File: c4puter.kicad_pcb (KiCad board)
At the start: 6 copper layers, 200 x 200 mm, 252 parts, among them J1 PDI, J2 MICROSD, J7 19V 3A, J8 DEBUG, Q1 AOD4189, Q2 AOD4189, Q3 2N7002, Q4 DMN3016LDN, Q5 DMN3016LDN, Q6 ULN2003APWR, Q7 ULN2003APWR, Q8 DMN3016LDN, Q9 DMN3018SSS, SW1 POWER, SW2 SW, U1 ATXMEGA8E5-MU, U4 TPIC6B595DW

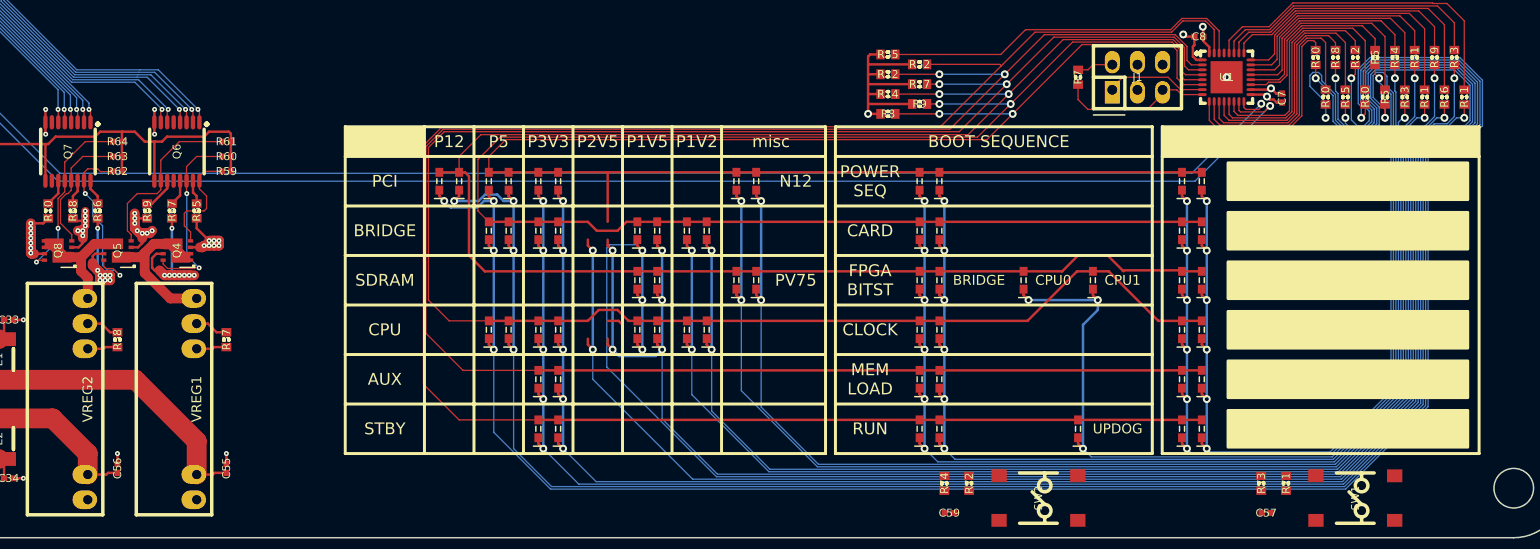
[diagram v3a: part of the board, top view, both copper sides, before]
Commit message: Delete extra column of LEDs
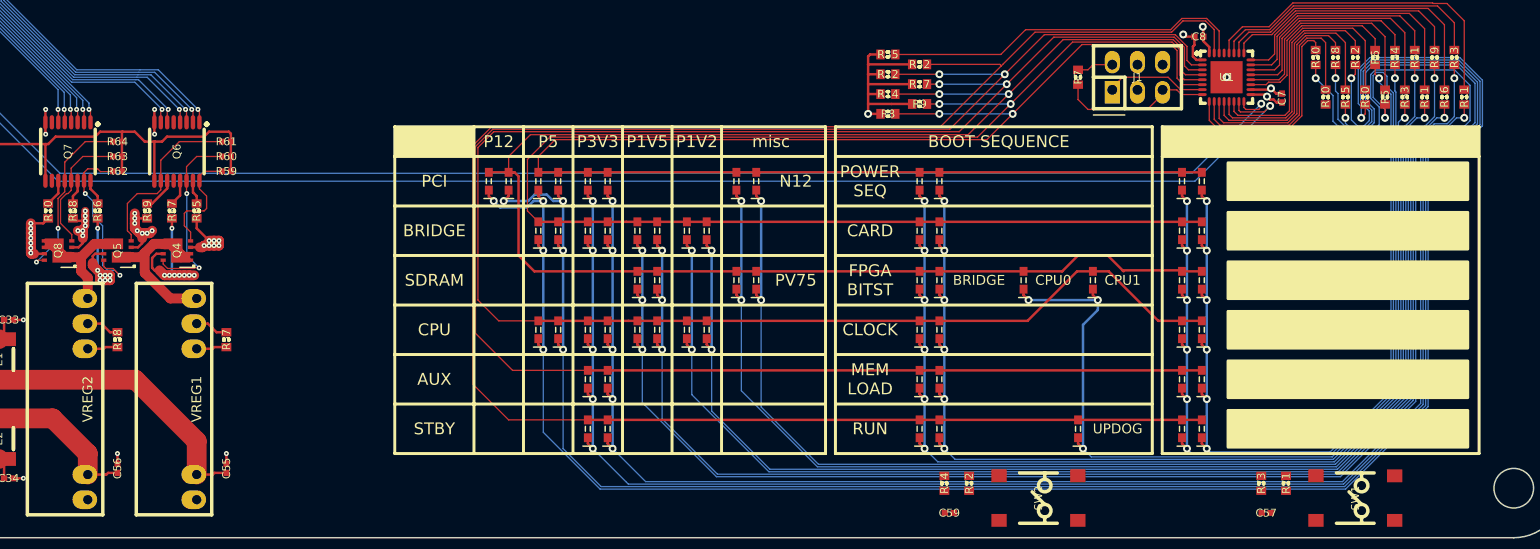
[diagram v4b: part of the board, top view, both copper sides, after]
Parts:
- moved DS1 5.00 mm to (91.5, 164.0)
- moved DS10 5.00 mm to (101.5, 169.0)
- moved DS11 5.00 mm to (101.5, 179.0)
- moved DS12 5.00 mm to (101.5, 184.0)
- moved DS13 5.00 mm to (101.5, 189.0)
- moved DS14 5.00 mm to (103.5, 164.0)
- moved DS15 5.00 mm to (103.5, 169.0)
- moved DS16 5.00 mm to (103.5, 179.0)
- moved DS17 5.00 mm to (103.5, 184.0)
- moved DS18 5.00 mm to (103.5, 189.0)
- moved DS2 5.00 mm to (93.5, 164.0)
- moved DS3 5.00 mm to (96.5, 164.0)
- moved DS4 5.00 mm to (96.5, 169.0)
- moved DS5 5.00 mm to (96.5, 179.0)
- moved DS6 5.00 mm to (98.5, 164.0)
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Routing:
- net /Blinkenlights/COL4: track 177.1 -> 0.00 mm, vias 3 -> 0
- net /Blinkenlights/COL6: track 153.6 -> 135.4 mm, vias 6 -> 4
- net /Blinkenlights/ROW4: track 201.2 -> 185.0 mm
- net /Blinkenlights/COL5: track 183.5 -> 167.8 mm
- net /Blinkenlights/ROW0: track 170.5 -> 155.5 mm
- net /Blinkenlights/ROW3: track 192.7 -> 181.8 mm
- net /Blinkenlights/ROW1: track 169.1 -> 158.3 mm
- net /Blinkenlights/ROW2: track 183.1 -> 173.1 mm
- net /Blinkenlights/ROW5: track 199.6 -> 189.6 mm
- net /Blinkenlights/COL1: track 197.2 -> 192.2 mm
- net /Blinkenlights/COL3: track 186.5 -> 181.5 mm
- net /Blinkenlights/COL2: track 184.7 -> 179.7 mm
- net /Blinkenlights/COL0: track 191.6 -> 186.6 mm
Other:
- board text removed: "P2V5"

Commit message: workworkwork
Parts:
- removed R14, R17, R22, R52, R55, R8, R9: 51k, IPC7351-Nominal:RESC1608X50
- added C82: 1u, IPC7351-Nominal:CAPC1005X55, F.Cu at (136.5, 134.5)
- added C83: 1u, IPC7351-Nominal:CAPC1005X55, F.Cu at (194.2, 130.5)
- added C84: 1u, IPC7351-Nominal:CAPC1005X55, F.Cu at (190.5, 130.5)
- added C85: 1u, IPC7351-Nominal:CAPC1005X55, F.Cu at (191.8, 130.5)
- added C86: 1u, IPC7351-Nominal:CAPC1005X55, F.Cu at (193.0, 130.5)
- added C87: 1u, IPC7351-Nominal:CAPC1005X55, F.Cu at (195.5, 138.5)
- added C88: 1u, IPC7351-Nominal:CAPC1005X55, F.Cu at (54.2, 21.5)
- added C89: 1u, IPC7351-Nominal:CAPC1005X55, F.Cu at (54.2, 19.2)
- added JP1: JUMPER-SOLDER, conn-test:JUMPER-SOLDER-SMD, F.Cu at (192.0, 100.0)
- added JP10: JUMPER-SOLDER, conn-test:JUMPER-SOLDER-SMD, F.Cu at (120.0, 115.0)
- added JP11: JUMPER-SOLDER, conn-test:JUMPER-SOLDER-SMD, F.Cu at (120.0, 118.0)
- added JP12: JUMPER-SOLDER, conn-test:JUMPER-SOLDER-SMD, F.Cu at (171.0, 100.5)
- added JP13: JUMPER-SOLDER, conn-test:JUMPER-SOLDER-SMD, F.Cu at (120.0, 112.0)
- added JP2: JUMPER-SOLDER, conn-test:JUMPER-SOLDER-SMD, F.Cu at (159.0, 100.5)
- added JP3: JUMPER-SOLDER, conn-test:JUMPER-SOLDER-SMD, F.Cu at (186.5, 100.0)
- added JP4: JUMPER-SOLDER, conn-test:JUMPER-SOLDER-SMD, F.Cu at (44.0, 101.0)
- added JP5: JUMPER-SOLDER, conn-test:JUMPER-SOLDER-SMD, F.Cu at (44.0, 97.0)
- added JP6: JUMPER-SOLDER, conn-test:JUMPER-SOLDER-SMD, F.Cu at (44.0, 105.0)
- added JP7: JUMPER-SOLDER, conn-test:JUMPER-SOLDER-SMD, F.Cu at (195.0, 100.0)
- added JP8: JUMPER-SOLDER, conn-test:JUMPER-SOLDER-SMD, F.Cu at (132.0, 100.0)
- added JP9: JUMPER-SOLDER, conn-test:JUMPER-SOLDER-SMD, F.Cu at (147.0, 100.5)
- added Q10: AOD514, smd-semi:TO-252, F.Cu at (180.3, 117.0)
- added Q11: AOD514, smd-semi:TO-252, F.Cu at (167.0, 118.0)
- added R75: 100k, IPC7351-Nominal:RESC1005X40, F.Cu at (150.0, 144.5)
- added R76: 100k, IPC7351-Nominal:RESC1005X40, F.Cu at (151.5, 144.5)
- added R77: R01, IPC7351-Nominal:RESC2012X50, F.Cu at (192.0, 104.0)
- added R78: R001, manuf:VISHAY-WSL3637-LARGE, F.Cu at (153.0, 107.0)
- added R79: R001, manuf:VISHAY-WSL3637-LARGE, F.Cu at (180.0, 107.0)
- added R80: R20, IPC7351-Nominal:RESC2012X50, F.Cu at (195.0, 104.0)
- added R81: R01, IPC7351-Nominal:RESC2012X50, F.Cu at (132.0, 104.0)
- added R82: R001, manuf:VISHAY-WSL3637-LARGE, F.Cu at (141.0, 107.0)
- added R83: R01, IPC7351-Nominal:RESC2012X50, F.Cu at (124.0, 115.0)
- added R84: R001, manuf:VISHAY-WSL3637-LARGE, F.Cu at (165.0, 107.0)
- added R85: 1k, IPC7351-Nominal:RESC1005X40, F.Cu at (190.5, 133.0)
- added U2: PCF8575, IPC7351-Nominal:SOP65P775X200-24, F.Cu at (140.0, 140.0)
- added U3: PCF8523TK, IPC7351-Nominal:SON80P400X400X80-9, F.Cu at (194.5, 134.5)
- added U5: CDCE913PW, IPC7351-Nominal:SOP65P640X120-14, F.Cu at (59.1, 19.3)
- added W1: NET-TIE, conn-test:NET-TIE-0.2mm, B.Cu at (33.8, 190.6)
- added W2: NET-TIE, conn-test:NET-TIE-0.2mm, B.Cu at (33.4, 178.6)
- added W3: NET-TIE, conn-test:NET-TIE-0.2mm, B.Cu at (33.8, 166.6)
- added W4: NET-TIE, conn-test:NET-TIE-0.2mm, B.Cu at (33.4, 156.6)
- added W5: NET-TIE, conn-test:NET-TIE-0.2mm, B.Cu at (33.5, 148.5)
- added X1: 32768, manuf:CITIZEN-CM130, F.Cu at (194.5, 140.5)
- added X2: 20MHz, IPC7351-Nominal:XTAL1200X480X460, F.Cu at (59.0, 13.1)
- Q4, Q5: value DMN3016LDN -> 2N7002; footprint manuf:DIODES-V-DFN3030-8 -> smd-semi:SOT-23
- Q6: value ULN2003APWR -> 2N7002; footprint IPC7351-Nominal:SOP65P640X120-16 -> smd-semi:SOT-23
- Q8: value DMN3016LDN -> ULN2003APWR; footprint manuf:DIODES-V-DFN3030-8 -> IPC7351-Nominal:SOP65P640X120-16
- Q9: value DMN3018SSS -> AOD417; footprint IPC7351-Nominal:SOIC127P600X175-8 -> smd-semi:TO-252
- R59, R60, R61: value 330k -> 0R
- R62, R63, R64: value 330k -> 120; footprint IPC7351-Nominal:RESC1005X40 -> IPC7351-Nominal:RESC1608X50
- R65, R66, R67, R69, R70: value 100 -> 120
- R68: value 100 -> 100k; footprint IPC7351-Nominal:RESC1608X50 -> IPC7351-Nominal:RESC1005X40
- U4: value TPIC6B595DW -> TLV70218DBV; footprint IPC7351-Nominal:SOIC127P1030X265-20 -> smd-semi:SOT-23-5
- moved U4 201.8 mm to (51.2, 20.2)
- moved Q9 155.0 mm to (190.0, 114.0), turned to 90 degrees
- moved R70 116.9 mm to (160.5, 139.0), turned to 180 degrees
- moved Q8 108.8 mm to (150.0, 133.0), turned to 0 degrees
- moved R69 107.8 mm to (160.5, 137.0), turned to 180 degrees
- moved R66 107.7 mm to (157.0, 143.0), turned to 180 degrees
- moved R62 107.6 mm to (157.0, 132.0), turned to 180 degrees
- moved R63 105.9 mm to (157.0, 137.0), turned to 180 degrees
- moved R64 105.1 mm to (157.0, 139.0), turned to 180 degrees
- moved R67 104.3 mm to (157.0, 130.0), turned to 180 degrees
- moved Q7 103.2 mm to (150.0, 140.0), turned to 0 degrees
- moved R68 101.5 mm to (148.5, 144.5)
- moved R65 98.5 mm to (157.0, 141.0), turned to 180 degrees
- moved Q5 93.5 mm to (138.0, 130.0)
- moved Q6 87.7 mm to (142.0, 130.0), turned to 90 degrees
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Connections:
- net /Power/3V3_2 renamed +3VB
- net /Power/5V_2 renamed +5VB
- net /Power/N12V renamed -12
- net N12_PCI renamed N12V_PCI
- net P12_PCI renamed P12V_PCI
- BRIDGE1 pad J10: P1V2_BRIDGE -> P1V2_CORE
- BRIDGE1 pad J12: P1V2_BRIDGE -> P1V2_CORE
- BRIDGE1 pad J14: P1V2_BRIDGE -> P1V2_CORE
- BRIDGE1 pad J8: P1V2_BRIDGE -> P1V2_CORE
- BRIDGE1 pad K11: P1V2_BRIDGE -> P1V2_CORE
- BRIDGE1 pad K13: P1V2_BRIDGE -> P1V2_CORE
- BRIDGE1 pad K9: P1V2_BRIDGE -> P1V2_CORE
- BRIDGE1 pad L10: P1V2_BRIDGE -> P1V2_CORE
- BRIDGE1 pad L12: P1V2_BRIDGE -> P1V2_CORE
- BRIDGE1 pad L14: P1V2_BRIDGE -> P1V2_CORE
- BRIDGE1 pad M11: P1V2_BRIDGE -> P1V2_CORE
- BRIDGE1 pad M13: P1V2_BRIDGE -> P1V2_CORE
- BRIDGE1 pad M9: P1V2_BRIDGE -> P1V2_CORE
- BRIDGE1 pad N10: P1V2_BRIDGE -> P1V2_CORE
- BRIDGE1 pad N12: P1V2_BRIDGE -> P1V2_CORE
- BRIDGE1 pad N14: P1V2_BRIDGE -> P1V2_CORE
- BRIDGE1 pad P11: P1V2_BRIDGE -> P1V2_CORE
- BRIDGE1 pad P13: P1V2_BRIDGE -> P1V2_CORE
- BRIDGE1 pad P9: P1V2_BRIDGE -> P1V2_CORE
- BRIDGE1 pad R14: P1V2_BRIDGE -> P1V2_CORE
- C33 pad 1: /Power/5V_1 -> +5VA
- C36 pad 1: P5_PCI -> P5V_PCI_A
- C37 pad 1: P3V3_PCI -> P3V3_PCI_A
- C38 pad 1: P3V3_PCI -> P3V3_PCI_A
- C40 pad 1: P5_PCI -> P5V_PCI_B
- C41 pad 1: P3V3_PCI -> P3V3_PCI_B
- C42 pad 1: P3V3_PCI -> P3V3_PCI_B
- C44 pad 1: P5_PCI -> P5V_PCI_A
- C45 pad 1: P3V3_PCI -> P3V3_PCI_A
- C46 pad 1: P3V3_PCI -> P3V3_PCI_A
- C48 pad 1: P5_PCI -> P5V_PCI_B
- C49 pad 1: P3V3_PCI -> P3V3_PCI_B
- C50 pad 1: P3V3_PCI -> P3V3_PCI_B
- C7 pad 2: SBY_P3V3 -> P3V3_STBY
- C71 pad 1: P5_PCI -> P5V_PCI_A
- C72 pad 1: P5_PCI -> P5V_PCI_B
- C73 pad 1: P5_PCI -> P5V_PCI_A
- C74 pad 1: P5_PCI -> P5V_PCI_B
- C8 pad 2: SBY_P3V3 -> P3V3_STBY
- C80 pad 1: P1V2_CPU -> P1V2_CORE
- C81 pad 1: P1V2_BRIDGE -> P1V5_BRIDGE
- CPU0 pad J10: P1V2_CPU -> P1V2_CORE
- CPU0 pad J12: P1V2_CPU -> P1V2_CORE
- CPU0 pad J14: P1V2_CPU -> P1V2_CORE
- CPU0 pad J8: P1V2_CPU -> P1V2_CORE
- CPU0 pad K11: P1V2_CPU -> P1V2_CORE
- CPU0 pad K13: P1V2_CPU -> P1V2_CORE
- CPU0 pad K9: P1V2_CPU -> P1V2_CORE
- CPU0 pad L10: P1V2_CPU -> P1V2_CORE
- CPU0 pad L12: P1V2_CPU -> P1V2_CORE
- CPU0 pad L14: P1V2_CPU -> P1V2_CORE
- CPU0 pad M11: P1V2_CPU -> P1V2_CORE
- CPU0 pad M13: P1V2_CPU -> P1V2_CORE
- CPU0 pad M9: P1V2_CPU -> P1V2_CORE
- CPU0 pad N10: P1V2_CPU -> P1V2_CORE
- CPU0 pad N12: P1V2_CPU -> P1V2_CORE
- CPU0 pad N14: P1V2_CPU -> P1V2_CORE
- CPU0 pad P11: P1V2_CPU -> P1V2_CORE
- CPU0 pad P13: P1V2_CPU -> P1V2_CORE
- CPU0 pad P9: P1V2_CPU -> P1V2_CORE
- CPU0 pad R14: P1V2_CPU -> P1V2_CORE
- CPU1 pad J10: P1V2_CPU -> P1V2_CORE
- CPU1 pad J12: P1V2_CPU -> P1V2_CORE
- CPU1 pad J14: P1V2_CPU -> P1V2_CORE
- CPU1 pad J8: P1V2_CPU -> P1V2_CORE
- CPU1 pad K11: P1V2_CPU -> P1V2_CORE
- CPU1 pad K13: P1V2_CPU -> P1V2_CORE
- CPU1 pad K9: P1V2_CPU -> P1V2_CORE
- CPU1 pad L10: P1V2_CPU -> P1V2_CORE
- CPU1 pad L12: P1V2_CPU -> P1V2_CORE
- CPU1 pad L14: P1V2_CPU -> P1V2_CORE
- CPU1 pad M11: P1V2_CPU -> P1V2_CORE
- CPU1 pad M13: P1V2_CPU -> P1V2_CORE
- CPU1 pad M9: P1V2_CPU -> P1V2_CORE
- CPU1 pad N10: P1V2_CPU -> P1V2_CORE
- CPU1 pad N12: P1V2_CPU -> P1V2_CORE
- CPU1 pad N14: P1V2_CPU -> P1V2_CORE
- CPU1 pad P11: P1V2_CPU -> P1V2_CORE
- CPU1 pad P13: P1V2_CPU -> P1V2_CORE
- CPU1 pad P9: P1V2_CPU -> P1V2_CORE
- CPU1 pad R14: P1V2_CPU -> P1V2_CORE
- E1 pad 1: /Power/5V_1 -> +5VA
- J1 pad 2: SBY_P3V3 -> P3V3_STBY
- LIMB1 pad 10: 3V3_LIMB -> P3V3_STBY
- LIMB1 pad 27: 3V3_LIMB -> P3V3_STBY
- LIMB1 pad 50: 3V3_LIMB -> P3V3_STBY
- LIMB1 pad 69: 3V3_LIMB -> P3V3_STBY
- LIMB1 pad 91: 3V3_LIMB -> P3V3_STBY
- LIMB1 pad 98: 3V3_LIMB -> P3V3_STBY
- PCI0 pad A10: P3V3_PCI -> P3V3_PCI_A
- PCI0 pad A14: P3V3_PCI_AUX -> P3V3_PCI_A
- PCI0 pad A16: P3V3_PCI -> P3V3_PCI_A
- PCI0 pad A21: P3V3_PCI -> P3V3_PCI_A
- PCI0 pad A27: P3V3_PCI -> P3V3_PCI_A
- PCI0 pad A33: P3V3_PCI -> P3V3_PCI_A
- PCI0 pad A39: P3V3_PCI -> P3V3_PCI_A
- PCI0 pad A45: P3V3_PCI -> P3V3_PCI_A
- PCI0 pad A5: P5_PCI -> P5V_PCI_A
- PCI0 pad A53: P3V3_PCI -> P3V3_PCI_A
- PCI0 pad A59: P3V3_PCI -> P3V3_PCI_A
- PCI0 pad A61: P5_PCI -> P5V_PCI_A
- PCI0 pad A62: P5_PCI -> P5V_PCI_A
- PCI0 pad A8: P5_PCI -> P5V_PCI_A
- PCI0 pad B19: P3V3_PCI -> P3V3_PCI_A
- PCI0 pad B25: P3V3_PCI -> P3V3_PCI_A
- PCI0 pad B31: P3V3_PCI -> P3V3_PCI_A
- PCI0 pad B36: P3V3_PCI -> P3V3_PCI_A
- PCI0 pad B41: P3V3_PCI -> P3V3_PCI_A
- PCI0 pad B43: P3V3_PCI -> P3V3_PCI_A
- PCI0 pad B5: P5_PCI -> P5V_PCI_A
- PCI0 pad B54: P3V3_PCI -> P3V3_PCI_A
- PCI0 pad B59: P3V3_PCI -> P3V3_PCI_A
- PCI0 pad B6: P5_PCI -> P5V_PCI_A
- PCI0 pad B61: P5_PCI -> P5V_PCI_A
- PCI0 pad B62: P5_PCI -> P5V_PCI_A
- PCI1 pad A10: P3V3_PCI -> P3V3_PCI_B
- PCI1 pad A14: P3V3_PCI_AUX -> P3V3_PCI_B
- PCI1 pad A16: P3V3_PCI -> P3V3_PCI_B
- PCI1 pad A21: P3V3_PCI -> P3V3_PCI_B
- PCI1 pad A27: P3V3_PCI -> P3V3_PCI_B
- PCI1 pad A33: P3V3_PCI -> P3V3_PCI_B
- PCI1 pad A39: P3V3_PCI -> P3V3_PCI_B
- PCI1 pad A45: P3V3_PCI -> P3V3_PCI_B
- PCI1 pad A5: P5_PCI -> P5V_PCI_B
- PCI1 pad A53: P3V3_PCI -> P3V3_PCI_B
- PCI1 pad A59: P3V3_PCI -> P3V3_PCI_B
- PCI1 pad A61: P5_PCI -> P5V_PCI_B
- PCI1 pad A62: P5_PCI -> P5V_PCI_B
- PCI1 pad A8: P5_PCI -> P5V_PCI_B
- PCI1 pad B19: P3V3_PCI -> P3V3_PCI_B
- PCI1 pad B25: P3V3_PCI -> P3V3_PCI_B
- PCI1 pad B31: P3V3_PCI -> P3V3_PCI_B
- PCI1 pad B36: P3V3_PCI -> P3V3_PCI_B
- PCI1 pad B41: P3V3_PCI -> P3V3_PCI_B
- PCI1 pad B43: P3V3_PCI -> P3V3_PCI_B
- PCI1 pad B5: P5_PCI -> P5V_PCI_B
- PCI1 pad B54: P3V3_PCI -> P3V3_PCI_B
- PCI1 pad B59: P3V3_PCI -> P3V3_PCI_B
- PCI1 pad B6: P5_PCI -> P5V_PCI_B
- PCI1 pad B61: P5_PCI -> P5V_PCI_B
- PCI1 pad B62: P5_PCI -> P5V_PCI_B
- PCI2 pad A10: P3V3_PCI -> P3V3_PCI_A
- PCI2 pad A14: P3V3_PCI_AUX -> P3V3_PCI_A
- PCI2 pad A16: P3V3_PCI -> P3V3_PCI_A
- PCI2 pad A21: P3V3_PCI -> P3V3_PCI_A
- PCI2 pad A27: P3V3_PCI -> P3V3_PCI_A
- PCI2 pad A33: P3V3_PCI -> P3V3_PCI_A
- PCI2 pad A39: P3V3_PCI -> P3V3_PCI_A
- PCI2 pad A45: P3V3_PCI -> P3V3_PCI_A
- PCI2 pad A5: P5_PCI -> P5V_PCI_A
- PCI2 pad A53: P3V3_PCI -> P3V3_PCI_A
- PCI2 pad A59: P3V3_PCI -> P3V3_PCI_A
- PCI2 pad A61: P5_PCI -> P5V_PCI_A
- PCI2 pad A62: P5_PCI -> P5V_PCI_A
- PCI2 pad A8: P5_PCI -> P5V_PCI_A
- PCI2 pad B19: P3V3_PCI -> P3V3_PCI_A
- PCI2 pad B25: P3V3_PCI -> P3V3_PCI_A
- PCI2 pad B31: P3V3_PCI -> P3V3_PCI_A
- PCI2 pad B36: P3V3_PCI -> P3V3_PCI_A
- PCI2 pad B41: P3V3_PCI -> P3V3_PCI_A
- PCI2 pad B43: P3V3_PCI -> P3V3_PCI_A
- PCI2 pad B5: P5_PCI -> P5V_PCI_A
- PCI2 pad B54: P3V3_PCI -> P3V3_PCI_A
- PCI2 pad B59: P3V3_PCI -> P3V3_PCI_A
- PCI2 pad B6: P5_PCI -> P5V_PCI_A
- PCI2 pad B61: P5_PCI -> P5V_PCI_A
- PCI2 pad B62: P5_PCI -> P5V_PCI_A
- PCI3 pad A10: P3V3_PCI -> P3V3_PCI_B
- PCI3 pad A14: P3V3_PCI_AUX -> P3V3_PCI_B
- PCI3 pad A16: P3V3_PCI -> P3V3_PCI_B
- PCI3 pad A21: P3V3_PCI -> P3V3_PCI_B
- PCI3 pad A27: P3V3_PCI -> P3V3_PCI_B
- PCI3 pad A33: P3V3_PCI -> P3V3_PCI_B
- PCI3 pad A39: P3V3_PCI -> P3V3_PCI_B
- PCI3 pad A45: P3V3_PCI -> P3V3_PCI_B
- PCI3 pad A5: P5_PCI -> P5V_PCI_B
- PCI3 pad A53: P3V3_PCI -> P3V3_PCI_B
- PCI3 pad A59: P3V3_PCI -> P3V3_PCI_B
- PCI3 pad A61: P5_PCI -> P5V_PCI_B
- PCI3 pad A62: P5_PCI -> P5V_PCI_B
- PCI3 pad A8: P5_PCI -> P5V_PCI_B
- PCI3 pad B19: P3V3_PCI -> P3V3_PCI_B
- PCI3 pad B25: P3V3_PCI -> P3V3_PCI_B
- PCI3 pad B31: P3V3_PCI -> P3V3_PCI_B
- PCI3 pad B36: P3V3_PCI -> P3V3_PCI_B
- PCI3 pad B41: P3V3_PCI -> P3V3_PCI_B
- PCI3 pad B43: P3V3_PCI -> P3V3_PCI_B
- PCI3 pad B5: P5_PCI -> P5V_PCI_B
- PCI3 pad B54: P3V3_PCI -> P3V3_PCI_B
- PCI3 pad B59: P3V3_PCI -> P3V3_PCI_B
- PCI3 pad B6: P5_PCI -> P5V_PCI_B
- PCI3 pad B61: P5_PCI -> P5V_PCI_B
- PCI3 pad B62: P5_PCI -> P5V_PCI_B
- Q3 pad 3: 3V3_LIMB -> P3V3_STBY
- Q4 pad 1: /Power/1V2OUT -> /Power/EN_SAFETY
- Q4 pad 2: Net-(Q4-Pad2) -> GND
- Q4 pad 3: Net-(Q4-Pad3) -> /Power/EN_P12V_PCI
- Q5 pad 1: /Power/1V2OUT -> /Power/EN_SAFETY
- Q5 pad 2: Net-(Q5-Pad2) -> GND
- Q5 pad 3: Net-(Q5-Pad3) -> /Power/EN_1V2
- Q6 pad 1: /Power/SW0 -> /Power/EN_SAFETY
- Q6 pad 2: /Power/SW1 -> GND
- Q6 pad 3: /Power/SW2 -> /Power/EN_1V5
- Q7 pad 1: /Power/SW6 -> /Power/EN_P12V_PCI
- Q7 pad 14: Net-(Q7-Pad14) -> Net-(Q11-Pad1)
- Q7 pad 15: Net-(Q5-Pad6) -> Net-(Q10-Pad1)
- Q7 pad 2: /Power/SW7 -> /Power/~EN_P5V_PCI_B
- Q7 pad 3: /Power/SW8 -> /Power/~EN_P3V3_S0B
- Q7 pad 4: /Power/SW9 -> /Power/DISCH_5VA
- Q7 pad 5: /Power/SW10 -> /Power/DISCH_5VB
- Q7 pad 6: /Power/SW11 -> /Power/DISCH_3VA
- Q7 pad 7: Net-(Q7-Pad7) -> /Power/DISCH_3VB
- Q8 pad 1: /Power/1V5OUT -> /Power/DISCH_1V5
- Q8 pad 2: Net-(Q8-Pad2) -> /Power/DISCH_1V2
- Q8 pad 3: Net-(Q7-Pad13) -> Net-(Q8-Pad3)
- Q8 pad 4: /Power/1V5OUT -> Net-(Q8-Pad4)
- Q8 pad 6: Net-(Q7-Pad12) -> Net-(Q8-Pad6)
- Q9 pad 1: Net-(Q9-Pad1) -> Net-(Q7-Pad16)
- Q9 pad 2: Net-(Q9-Pad1) -> +12
- Q9 pad 3: Net-(Q9-Pad1) -> Net-(Q9-Pad3)
- R27 pad 1: P3V3_PCI -> P3V3_BRIDGE
- R28 pad 1: P3V3_PCI -> P3V3_BRIDGE
- R29 pad 1: P3V3_PCI -> P3V3_BRIDGE
- R30 pad 1: P3V3_PCI -> P3V3_BRIDGE
- R31 pad 1: P3V3_PCI -> P3V3_BRIDGE
- R32 pad 1: P3V3_PCI -> P3V3_BRIDGE
- R33 pad 1: P3V3_PCI -> P3V3_BRIDGE
- R34 pad 1: P3V3_PCI -> P3V3_BRIDGE
- R35 pad 1: P3V3_PCI -> P3V3_BRIDGE
- R36 pad 1: P3V3_PCI -> P3V3_BRIDGE
- R37 pad 1: P3V3_PCI -> P3V3_BRIDGE
- R38 pad 1: P3V3_PCI -> P3V3_BRIDGE
- R39 pad 1: P3V3_PCI -> P3V3_AUX
- R40 pad 1: P3V3_PCI -> P3V3_AUX
- R41 pad 1: P3V3_PCI -> P3V3_AUX
- R42 pad 1: P3V3_PCI -> P3V3_AUX
- R43 pad 1: P3V3_PCI -> P3V3_AUX
- R44 pad 1: P3V3_PCI -> P3V3_AUX
- R45 pad 1: P3V3_PCI -> P3V3_AUX
- R46 pad 1: P3V3_PCI -> P3V3_AUX
- R47 pad 1: P3V3_PCI -> P3V3_AUX
- R48 pad 1: P3V3_PCI -> P3V3_AUX
- R49 pad 2: P3V3_PCI -> P3V3_AUX
- R59 pad 1: Net-(Q4-Pad3) -> Net-(R59-Pad1)
- R59 pad 2: +12 -> GND
- R60 pad 1: Net-(Q4-Pad6) -> Net-(R60-Pad1)
- R60 pad 2: +12 -> GND
- R61 pad 1: Net-(Q5-Pad3) -> Net-(R61-Pad1)
- R61 pad 2: +12 -> GND
- R62 pad 1: Net-(Q5-Pad6) -> +1V2
- R62 pad 2: +12 -> Net-(Q8-Pad15)
- R63 pad 1: Net-(Q7-Pad13) -> Net-(R63-Pad1)
- R63 pad 2: +12 -> Net-(Q7-Pad13)
- R64 pad 1: Net-(Q7-Pad12) -> Net-(R64-Pad1)
- R64 pad 2: +12 -> Net-(Q7-Pad12)
- R65 pad 1: Net-(Q4-Pad2) -> +3VA
- R65 pad 2: Net-(Q6-Pad15) -> Net-(Q7-Pad11)
- R66 pad 1: Net-(Q5-Pad5) -> Net-(Q11-Pad2)
- R66 pad 2: Net-(Q7-Pad16) -> Net-(Q7-Pad10)
- R67 pad 1: Net-(Q4-Pad5) -> +1V5
- R67 pad 2: Net-(Q6-Pad13) -> Net-(Q8-Pad16)
- R68 pad 1: Net-(Q8-Pad2) -> +12
- R68 pad 2: Net-(Q7-Pad14) -> Net-(Q7-Pad16)
- R69 pad 1: Net-(Q5-Pad2) -> +5VA
- R69 pad 2: Net-(Q6-Pad11) -> Net-(R63-Pad1)
- R7 pad 1: SBY_P3V3 -> P3V3_STBY
- R70 pad 1: Net-(Q8-Pad5) -> Net-(Q10-Pad2)
- R70 pad 2: Net-(Q7-Pad11) -> Net-(R64-Pad1)
- U1 pad 17: SBY_P3V3 -> P3V3_STBY
- U1 pad 32: SBY_P3V3 -> P3V3_STBY
- U4 pad 1: (no net) -> P3V3_AUX
- U4 pad 2: (no net) -> GND
- U4 pad 3: Net-(U4-Pad3) -> P3V3_AUX
- U4 pad 4: Net-(U4-Pad4) -> GND
- VREG1 pad 1: /Power/1V2OUT -> +1V2
- VREG1 pad 5: Net-(VREG1-Pad5) -> /Power/EN_1V2
- VREG2 pad 1: /Power/1V5OUT -> +1V5
- VREG2 pad 5: Net-(VREG2-Pad5) -> /Power/EN_1V5
- VRM1 pad B12: /Power/5V_1 -> +5VA
- VRM1 pad B13: /Power/5V_1 -> +5VA
- VRM1 pad B14: /Power/5V_1 -> +5VA
- VRM1 pad B15: /Power/5V_1 -> +5VA
- VRM1 pad B16: /Power/5V_1 -> +5VA
- VRM1 pad B17: /Power/5V_1 -> +5VA
- VRM1 pad B18: /Power/5V_1 -> +5VA
- VRM1 pad B33: /Power/3V3_1 -> +3VA
- VRM1 pad B34: /Power/3V3_1 -> +3VA
- VRM1 pad B35: /Power/3V3_1 -> +3VA
- VRM1 pad B36: /Power/3V3_1 -> +3VA
- VRM1 pad B37: /Power/3V3_1 -> +3VA
- VRM1 pad B38: /Power/3V3_1 -> +3VA
- VRM1 pad B39: /Power/3V3_1 -> +3VA
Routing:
- net +3VA: track 0.00 -> 302.2 mm, vias 0 -> 40
- net +5VA: track 0.00 -> 291.5 mm, vias 0 -> 38
- net P3V3_AUX: track 3.19 -> 293.8 mm, vias 1 -> 16
- net /Power/SW3: track 224.7 -> 0.00 mm, vias 1 -> 0
- net /Power/SW2: track 224.6 -> 0.00 mm, vias 1 -> 0
- net /Power/SW1: track 224.5 -> 0.00 mm, vias 1 -> 0
- net /Power/SW5: track 224.4 -> 0.00 mm, vias 1 -> 0
- net /Power/SW0: track 224.4 -> 0.00 mm, vias 1 -> 0
- net /Power/SW4: track 224.3 -> 0.00 mm, vias 1 -> 0
- net +3VB: track 0.00 -> 222.0 mm, vias 0 -> 36
- net /Power/SW11: track 219.4 -> 0.00 mm, vias 1 -> 0
- net /Power/SW10: track 219.2 -> 0.00 mm, vias 1 -> 0
- net /Power/SW9: track 218.9 -> 0.00 mm, vias 1 -> 0
- net /Power/SW8: track 218.7 -> 0.00 mm, vias 1 -> 0
- net /Power/SW7: track 218.4 -> 0.00 mm, vias 1 -> 0
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- added copper zone on B.Cu, net +3VA
- added copper zone on F.Cu, net +3VA
- added copper zone on B.Cu, net +3VB
- added copper zone on F.Cu, net +3VB
- added copper zone on B.Cu, net +5VA
- added copper zone on F.Cu, net +5VA
- added copper zone on B.Cu, net +5VB
- added copper zone on F.Cu, net +5VB
- added copper zone on F.Cu, net GND
- added copper zone on B.Cu, net P12_PCI
- added copper zone on In3.Cu, net P1V2_CPU
- added copper zone on In4.Cu, net P1V5_BRIDGE
- added copper zone on In2.Cu, net P3V3_CPU
- added copper zone on F.Cu, net P3V3_PCI_A
- added copper zone on In2.Cu, net P3V3_PCI_A
- added copper zone on F.Cu, net P3V3_PCI_B
- added copper zone on In4.Cu, net P3V3_PCI_B
- added copper zone on B.Cu, net P5V_PCI_A
- added copper zone on F.Cu, net P5V_PCI_A
- added copper zone on F.Cu, net P5V_PCI_B
- removed copper zone on B.Cu, net P12V_PCI
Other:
- board text added: "I2C RTC PCF8523 ADDR 0xD0"
